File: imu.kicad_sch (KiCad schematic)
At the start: 2 parts, among them U2 BMP581, U3 BNO085

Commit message: Added todo list
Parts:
- removed U3: BNO085, BNO085:IC_BNO085, symbol BNO085:BNO085
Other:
- note added: "TODO list: - Add the stemma qt adapter for the BNO085 - Add the BMP581 connections - Add UART to GPS Neo m9n module - Add ADXL345 and ADXL 375 via I2C"

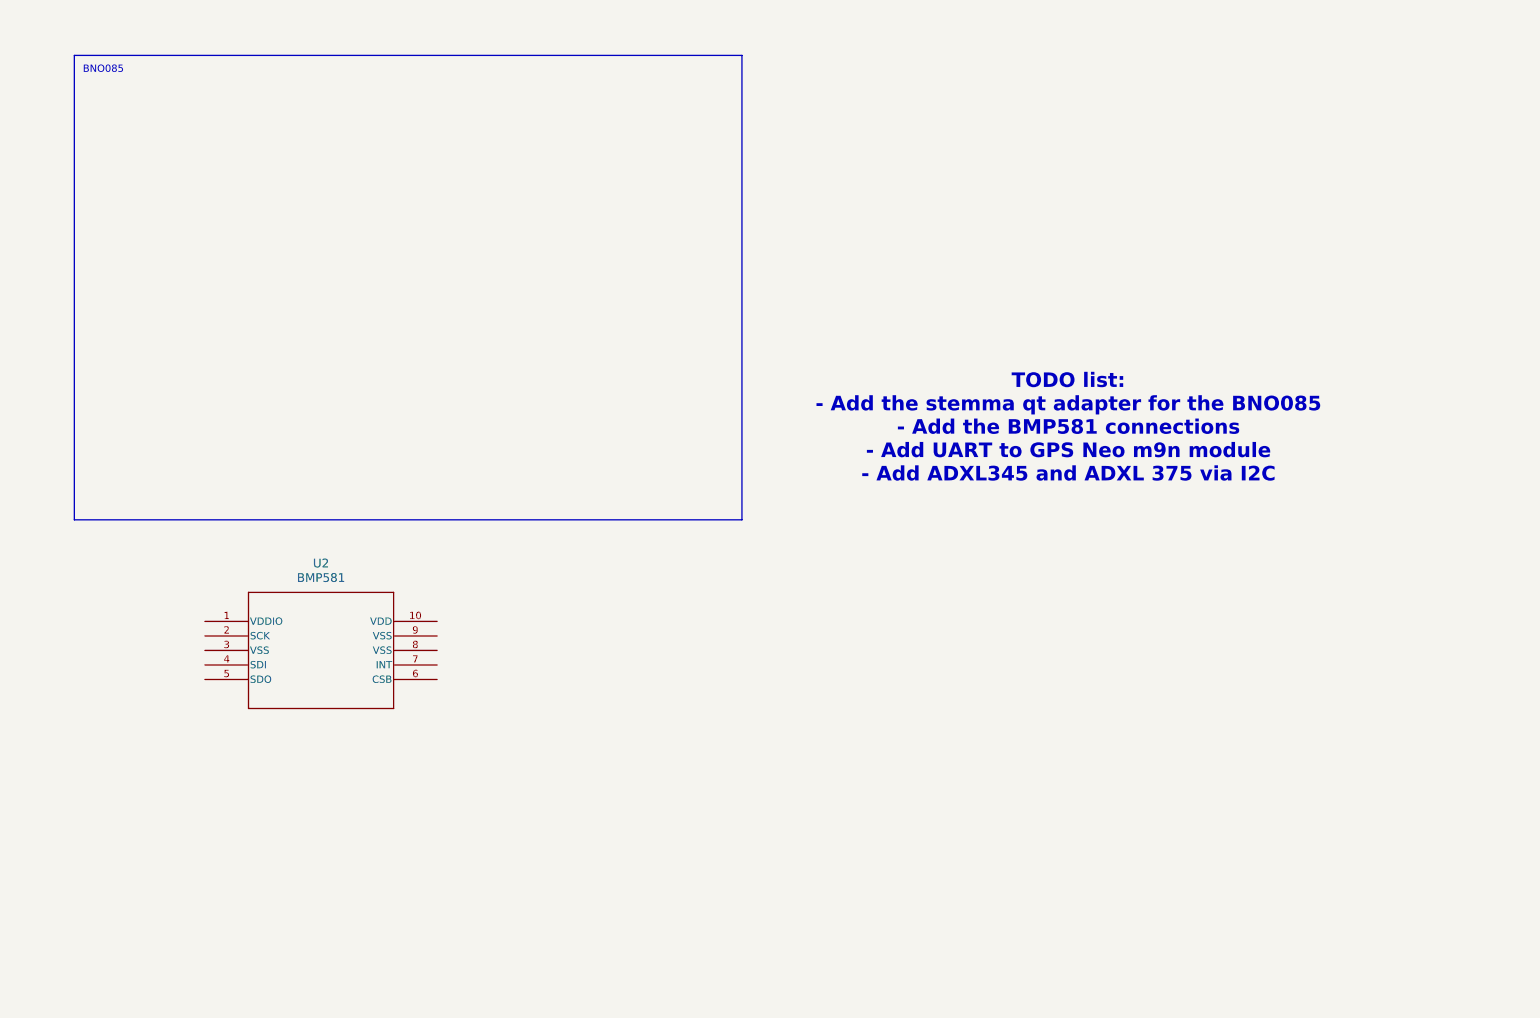
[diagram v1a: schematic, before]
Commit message: Modified schematics for IMUs
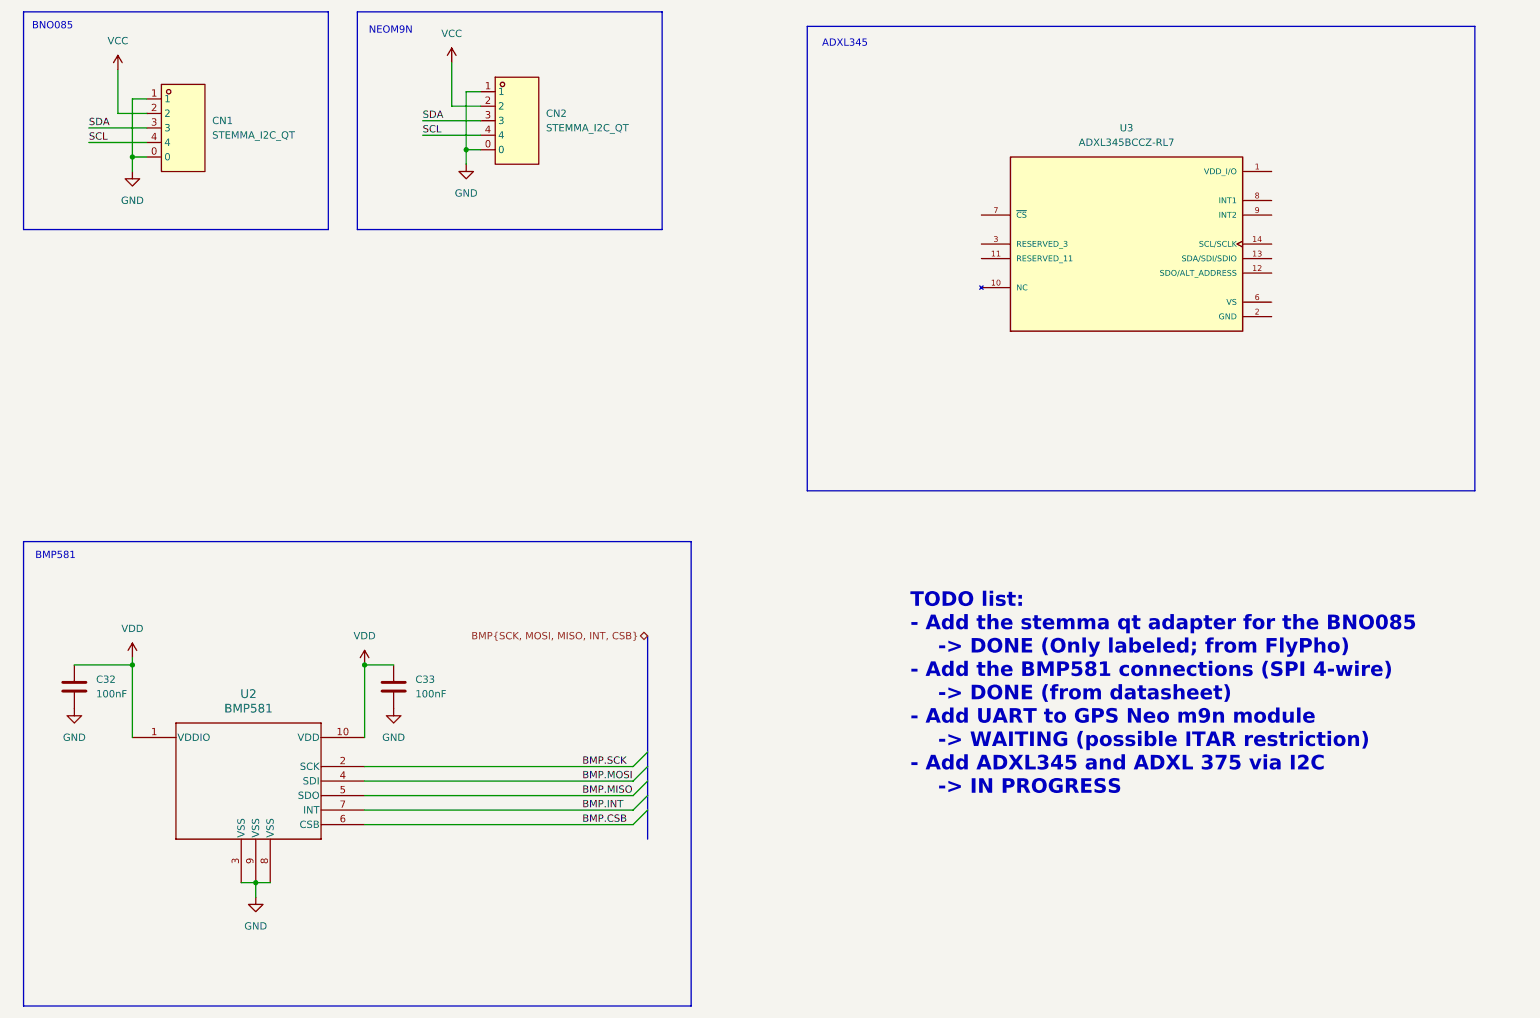
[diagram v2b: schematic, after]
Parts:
- added C32, C33: 100nF, symbol Device:C
- added CN1, CN2: STEMMA_I2C_QT, easyeda2kicad:CONN-SMD_BM04B-SRSS-TB, symbol CONN-SMD_BM04B-SRSS-TB:BM04B-SRSS-TB(LF)(SN)
- added U3: ADXL345BCCZ-RL7, ADXL345BCCZ-RL7:PQFN80P500X300X100-14N, symbol ADXL345BCCZ-RL7:ADXL345BCCZ-RL7
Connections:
- net VDD: now reaches U2.1 (VDDIO)
- net VDD: now also U2.10 (VDD), C32.1, C33.1
- net BMP.SCK: now reaches U2.2 (SCK)
- net GND: now reaches U2.3 (VSS)
- net GND: now also U2.8 (VSS), U2.9 (VSS), C32.2, C33.2, CN1.0, CN1.1, CN2.0, CN2.1, U3.2 (GND), U3.4 (GND), U3.5 (GND)
- net BMP.MOSI: now reaches U2.4 (SDI)
- net BMP.MISO: now reaches U2.5 (SDO)
- net BMP.CSB: now reaches U2.6 (CSB)
- net BMP.INT: now reaches U2.7 (INT)
- new net SCL: CN1.4, CN2.4
- new net SDA: CN1.3, CN2.3
- new net VCC: CN1.2, CN2.2
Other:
- note added: "ADXL345"
- note added: "BMP581"
- note added: "NEOM9N"
- note added: "TODO list: - Add the stemma qt adapter for the BNO085 -> DONE (Only labeled; from FlyPho) - Add the BMP581 connections (SPI 4-wire) -> DONE (from datasheet) - Add UART to GPS Neo m9n module -> WAITING (possible ITAR restriction) - Add ADXL345 and ADXL 375 via I2C -> IN PROGRESS"
- note removed: "TODO list: - Add the stemma qt adapter for the BNO085 - Add the BMP581 connections - Add UART to GPS Neo m9n module - Add ADXL345 and ADXL 375 via I2C"
- moved on the sheet: U2

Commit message: Power Schematic semi-finalized
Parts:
- added CIO (x2), CS (x2): C, symbol Device:C
- added U5: ADXL375BCCZ-RL7, easyeda2kicad:LGA-14_L5.0-W3.0-P0.80-BL, symbol ADXL375:ADXL375BCCZ-RL7
- CN1, CN2: value STEMMA_I2C_QT -> STE_I2C_QT
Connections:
- net GND: now also CIO.2, CS.2, U5.2 (GND), U5.4 (GND), U5.5 (GND)
- net VDD: now also U3.1 (VDD_I/O), U3.6 (VS), CIO.1, CIO.1, CS.1, CS.1, U5.1 (VDDI/O), U5.6 (VS)
- net ADXL345.SDO: now reaches U3.12 (SDO/ALT_ADDRESS)
- net ADXL345.SDO: now also U5.12 (SDO/ALTADDRESS)
- net ADXL345.SDI: now reaches U3.13 (SDA/SDI/SDIO)
- net ADXL345.SDI: now also U5.13 (SDA/SDI/SDIO)
- net ADXL345.SCLK: now reaches U3.14 (SCL/SCLK)
- net ADXL345.SCLK: now also U5.14 (SCL/SCLK)
- net ADXL345.CS: now reaches U3.7 (~{CS})
- net ADXL345.CS: now also U5.7 (~{CS})
- net SCL renamed BNO085.SCL
- net BNO085.SCL: no longer CN2.4
- net SDA renamed BNO085.SDA
- net BNO085.SDA: no longer CN2.3
- new net NEOM9N.SCL: CN2.4
- new net NEOM9N.SDA: CN2.3
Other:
- note added: "TODO list: - Add the stemma qt adapter for the BNO085 -> DONE (Only labeled; from FlyPho) - Add the BMP581 connections (SPI 4-wire) -> DONE (from datasheet) - Add UART to GPS Neo m9n module -> WAITING (possible ITAR restriction) - Add ADXL345 and ADXL 375 via SPI -> IN PROGRESS"
- note removed: "TODO list: - Add the stemma qt adapter for the BNO085 -> DONE (Only labeled; from FlyPho) - Add the BMP581 connections (SPI 4-wire) -> DONE (from datasheet) - Add UART to GPS Neo m9n module -> WAITING (possible ITAR restriction) - Add ADXL345 and ADXL 375 via I2C -> IN PROGRESS"
- moved on the sheet: CN1, CN2, U3
